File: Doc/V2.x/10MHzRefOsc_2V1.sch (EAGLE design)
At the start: 82 parts, among them CON1 TYCO-AMP_USBUSB-B_SMT, CON2 HEADER-2X5SMD, CON3 SD-73100-0105, CON4 AVR-ISP-6SMD, CON5 AVR-JTAG-10SMD, CON6 HEADER-2X3SMD, CON7 MCX-J-P-X-RA-SM1, IC1 ATmega328-P, IC2 LC4032V_XXT44, IC3 74HCT221D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

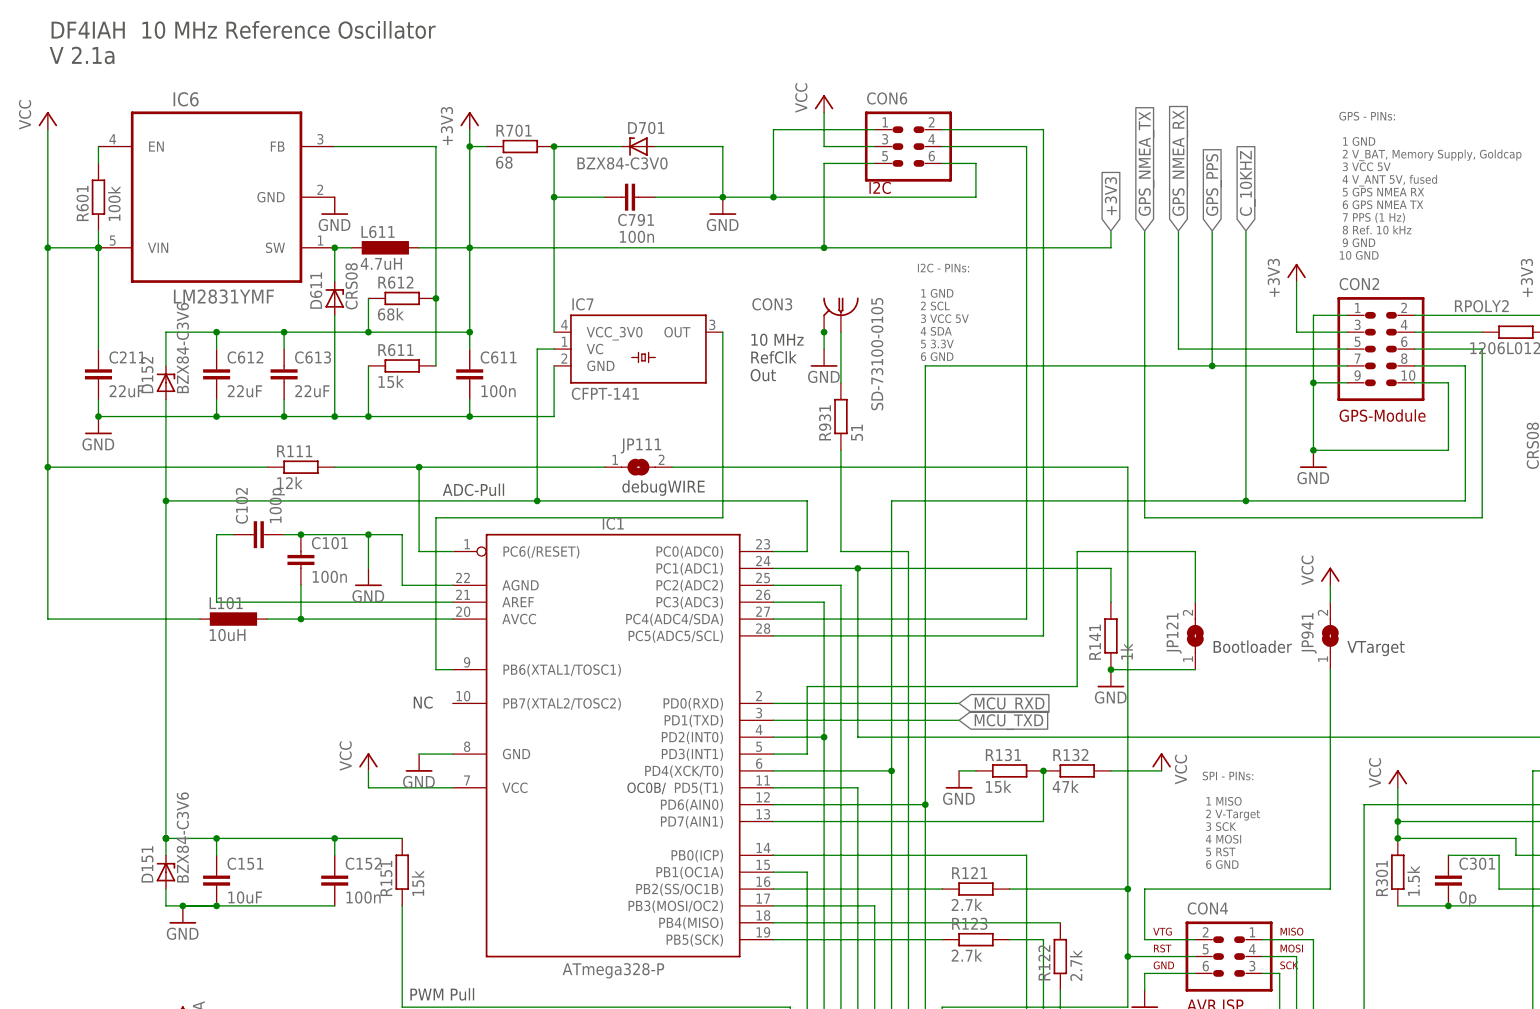
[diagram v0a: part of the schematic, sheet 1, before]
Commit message: avr_DF4IAH_Bootloader - Doc - Eagle: 2.1 - 3.3V adjusting resistors corrected, 2-way jumpers now THT instead of SMT
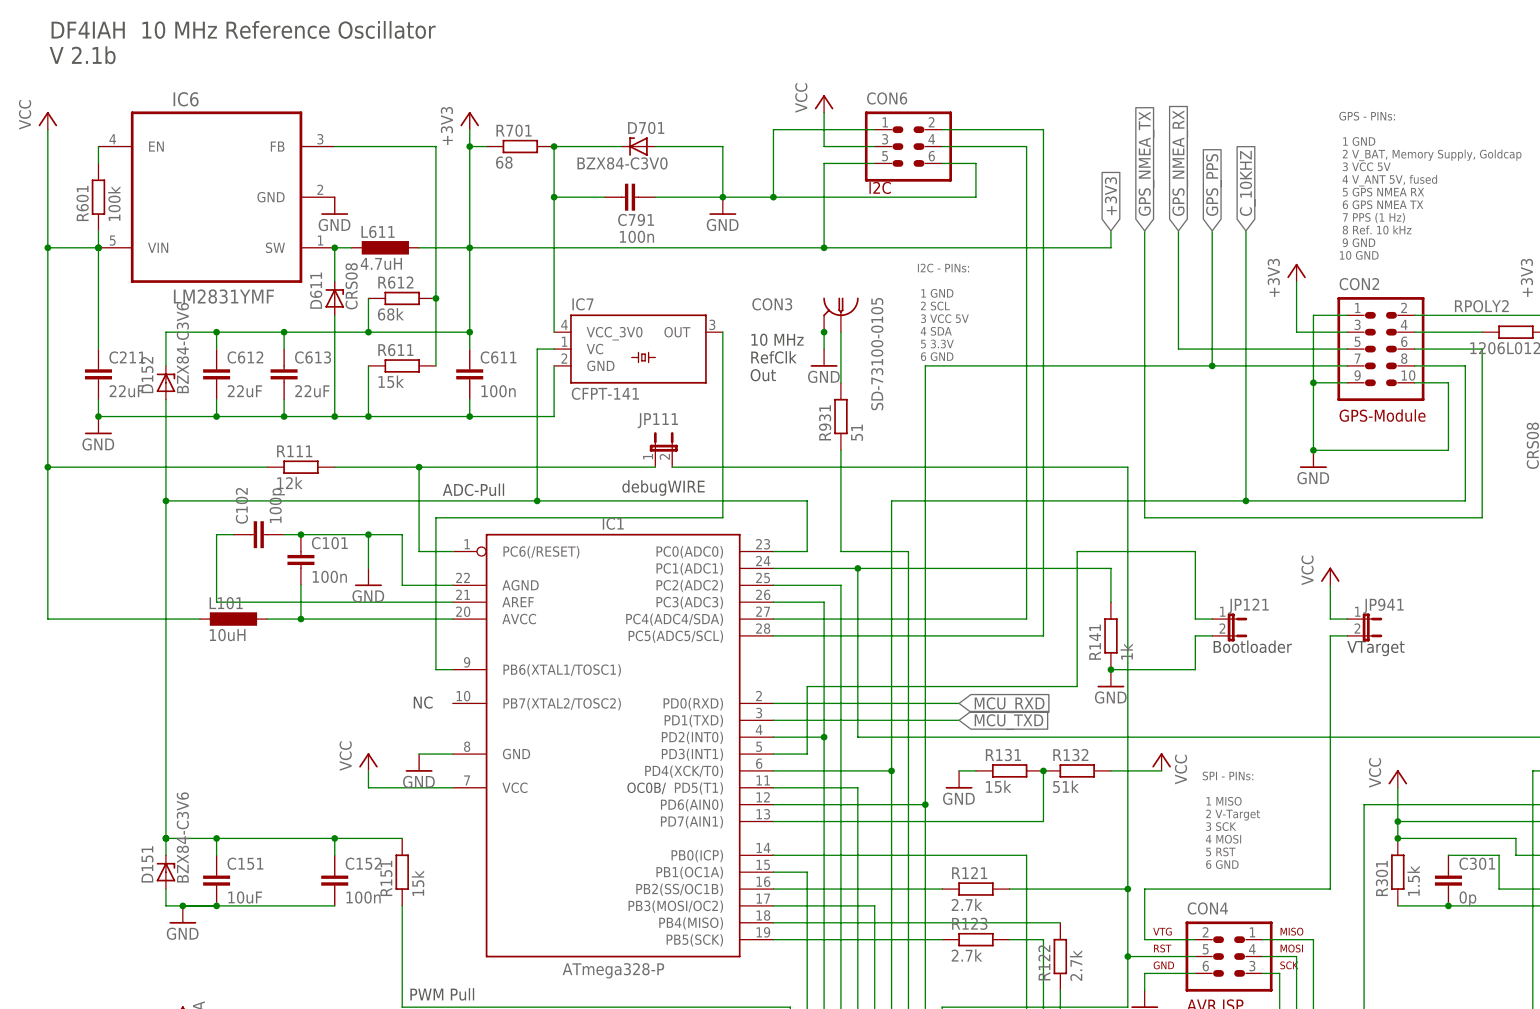
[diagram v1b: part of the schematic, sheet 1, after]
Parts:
- JP111, JP121, JP941: device jumper:SJW -> jumper:JP1E
- R132: value 47k -> 51k
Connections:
- net GND: now also JP121.2; no longer JP121.1
- net INT1: now also JP121.1; no longer JP121.2
- net ISP_VTARGET: now also JP941.2; no longer JP941.1
- net VCC: now also JP941.1; no longer JP941.2
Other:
- note added: "DF4IAH 10 MHz Reference Oscillator V 2.1b"
- note removed: "DF4IAH 10 MHz Reference Oscillator V 2.1a"
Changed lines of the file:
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@@
 <part name="RPOLY1" library="rcl" deviceset="R-EU_" device="M1206" value="1206L025YR_0.5A"/>
 <part name="RPOLY2" library="rcl" deviceset="R-EU_" device="M1206" value="1206L012WR_0.1A"/>
-<part name="JP111" library="jumper" deviceset="SJ" device="W"/>
-<part name="JP941" library="jumper" deviceset="SJ" device="W"/>
-<part name="JP121" library="jumper" deviceset="SJ" device="W"/>
 <part name="GND6" library="supply1" deviceset="GND" device=""/>
 <part name="CON2" library="df4iah" deviceset="HEADER-2X5" device="SMD"/>
@@
 <part name="R201" library="rcl" deviceset="R-EU_" device="R0805" value="2.7k"/>
 <part name="R131" library="rcl" deviceset="R-EU_" device="R0805" value="15k"/>
-<part name="R132" library="rcl" deviceset="R-EU_" device="R0805" value="47k"/>
+<part name="R132" library="rcl" deviceset="R-EU_" device="R0805" value="51k"/>
 <part name="R311" library="rcl" deviceset="R-EU_" device="R0805" value="4.3k"/>
 <part name="C612" library="rcl" deviceset="C-EU" device="C0805" value="22uF"/>
 <part name="C613" library="rcl" deviceset="C-EU" device="C0805" value="22uF"/>
 <part name="C211" library="rcl" deviceset="C-EU" device="C0805" value="22uF"/>
+<part name="JP941" library="jumper" deviceset="JP1E" device=""/>
+<part name="JP121" library="jumper" deviceset="JP1E" device=""/>
+<part name="JP111" library="jumper" deviceset="JP1E" device=""/>
 </parts>
 <sheets>
@@
 <text x="198.12" y="145.034" size="1.016" layer="97">2.5 MHz out</text>
 <text x="5.334" y="291.846" size="2.54" layer="97">DF4IAH  10 MHz Reference Oscillator
-V 2.1a</text>
+V 2.1b</text>
 <text x="59.436" y="144.018" size="1.778" layer="97">USB Disconnect</text>
 <text x="102.616" y="122.936" size="1.778" layer="97">USB D-</text>
@@
 <attribute name="VALUE" x="218.948" y="248.158" size="1.778" layer="96"/>
 </instance>
-<instance part="JP111" gate="1" x="93.98" y="231.14"/>
-<instance part="JP941" gate="1" x="198.12" y="205.74" rot="R90"/>
-<instance part="JP121" gate="1" x="177.8" y="205.74" rot="R90"/>
 <instance part="GND6" gate="1" x="170.18" y="149.86"/>
 <instance part="CON2" gate="G$1" x="205.74" y="248.92"/>
@@
 <instance part="C613" gate="G$1" x="40.64" y="246.38"/>
 <instance part="C211" gate="G$1" x="12.7" y="246.38"/>
+<instance part="JP941" gate="A" x="203.2" y="208.28" rot="R270"/>
+<instance part="JP121" gate="A" x="182.88" y="208.28" rot="R270"/>
+<instance part="JP111" gate="A" x="96.52" y="233.68" smashed="yes">
+<attribute name="NAME" x="93.98" y="237.49" size="1.778" layer="95"/>
+<attribute name="VALUE" x="102.235" y="233.68" size="1.778" layer="96" rot="R90"/>
+</instance>
 </instances>
 <busses>
@@
 <segment>
 <pinref part="GND10" gate="1" pin="GND"/>
-<pinref part="JP121" gate="1" pin="1"/>
 <wire x1="165.1" y1="200.66" x2="177.8" y2="200.66" width="0.1524" layer="91"/>
 <junction x="165.1" y="200.66"/>
 <pinref part="R141" gate="G$1" pin="1"/>
+<wire x1="177.8" y1="200.66" x2="177.8" y2="205.74" width="0.1524" layer="91"/>
+<pinref part="JP121" gate="A" pin="2"/>
+<wire x1="177.8" y1="205.74" x2="180.34" y2="205.74" width="0.1524" layer="91"/>
 </segment>
 <segment>
@@
 <segment>
 <pinref part="P+4" gate="VCC" pin="VCC"/>
-<pinref part="JP941" gate="1" pin="2"/>
-<wire x1="198.12" y1="213.36" x2="198.12" y2="210.82" width="0.1524" layer="91"/>
+<wire x1="198.12" y1="213.36" x2="198.12" y2="208.28" width="0.1524" layer="91"/>
+<pinref part="JP941" gate="A" pin="1"/>
+<wire x1="198.12" y1="208.28" x2="200.66" y2="208.28" width="0.1524" layer="91"/>
 </segment>
 <segment>
@@
 <wire x1="66.04" y1="218.44" x2="60.96" y2="218.44" width="0.1524" layer="91"/>
 <wire x1="60.96" y1="218.44" x2="60.96" y2="231.14" width="0.1524" layer="91"/>
-<wire x1="60.96" y1="231.14" x2="88.9" y2="231.14" width="0.1524" layer="91"/>
+<wire x1="60.96" y1="231.14" x2="96.52" y2="231.14" width="0.1524" layer="91"/>
 <junction x="60.96" y="231.14"/>
-<pinref part="JP111" gate="1" pin="1"/>
 <pinref part="R111" gate="G$1" pin="2"/>
+<pinref part="JP111" gate="A" pin="1"/>
 </segment>
 </net>
 <net name="ISP_VTARGET" class="0">
 <segment>
-<pinref part="JP941" gate="1" pin="1"/>
 <pinref part="CON4" gate="G$1" pin="2"/>
-<wire x1="198.12" y1="167.64" x2="198.12" y2="200.66" width="0.1524" layer="91"/>
+<wire x1="198.12" y1="167.64" x2="198.12" y2="205.74" width="0.1524" layer="91"/>
 <wire x1="177.8" y1="160.02" x2="170.18" y2="160.02" width="0.1524" layer="91"/>
 <wire x1="170.18" y1="160.02" x2="170.18" y2="167.64" width="0.1524" layer="91"/>
 <wire x1="170.18" y1="167.64" x2="198.12" y2="167.64" width="0.1524" layer="91"/>
+<pinref part="JP941" gate="A" pin="2"/>
+<wire x1="198.12" y1="205.74" x2="200.66" y2="205.74" width="0.1524" layer="91"/>
 </segment>
 </net>
@@
 <net name="INT1" class="0">
 <segment>
-<wire x1="177.8" y1="210.82" x2="177.8" y2="218.44" width="0.1524" layer="91"/>
+<wire x1="177.8" y1="208.28" x2="177.8" y2="218.44" width="0.1524" layer="91"/>
 <wire x1="177.8" y1="218.44" x2="160.02" y2="218.44" width="0.1524" layer="91"/>
 <wire x1="160.02" y1="218.44" x2="160.02" y2="198.12" width="0.1524" layer="91"/>
@@
 <wire x1="119.38" y1="198.12" x2="119.38" y2="187.96" width="0.1524" layer="91"/>
 <wire x1="119.38" y1="187.96" x2="114.3" y2="187.96" width="0.1524" layer="91"/>
-<pinref part="JP121" gate="1" pin="2"/>
+<pinref part="JP121" gate="A" pin="1"/>
+<wire x1="177.8" y1="208.28" x2="180.34" y2="208.28" width="0.1524" layer="91"/>
 </segment>
 </net>
@@
 <net name="JTAG_SRST" class="0">
 <segment>
-<pinref part="JP111" gate="1" pin="2"/>
 <wire x1="99.06" y1="231.14" x2="167.64" y2="231.14" width="0.1524" layer="91"/>
 <wire x1="149.86" y1="167.64" x2="167.64" y2="167.64" width="0.1524" layer="91"/>
@@
 <wire x1="167.64" y1="157.48" x2="177.8" y2="157.48" width="0.1524" layer="91"/>
 <junction x="167.64" y="157.48"/>
-</segment>
-</net>
+<pinref part="JP111" gate="A" pin="2"/>
+</segment>
+</net>
